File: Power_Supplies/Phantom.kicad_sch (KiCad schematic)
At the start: 24 parts, among them IC9 LT8338, J3 XLR3, SW1 SW_Push

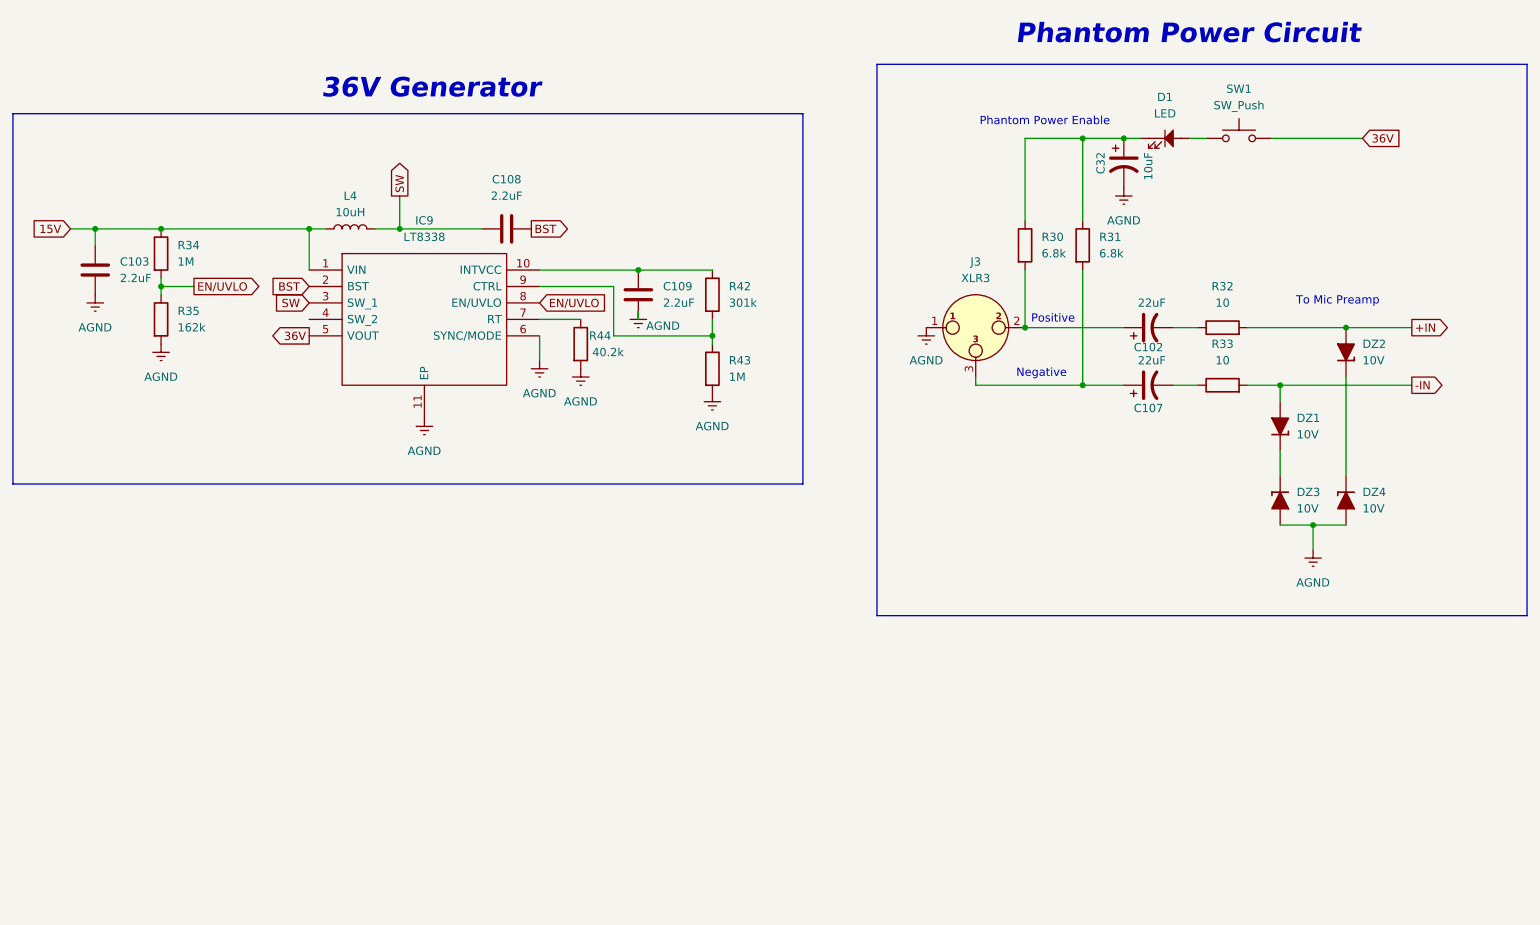
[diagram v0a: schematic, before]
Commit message: Started preamp design (finished stage 1)
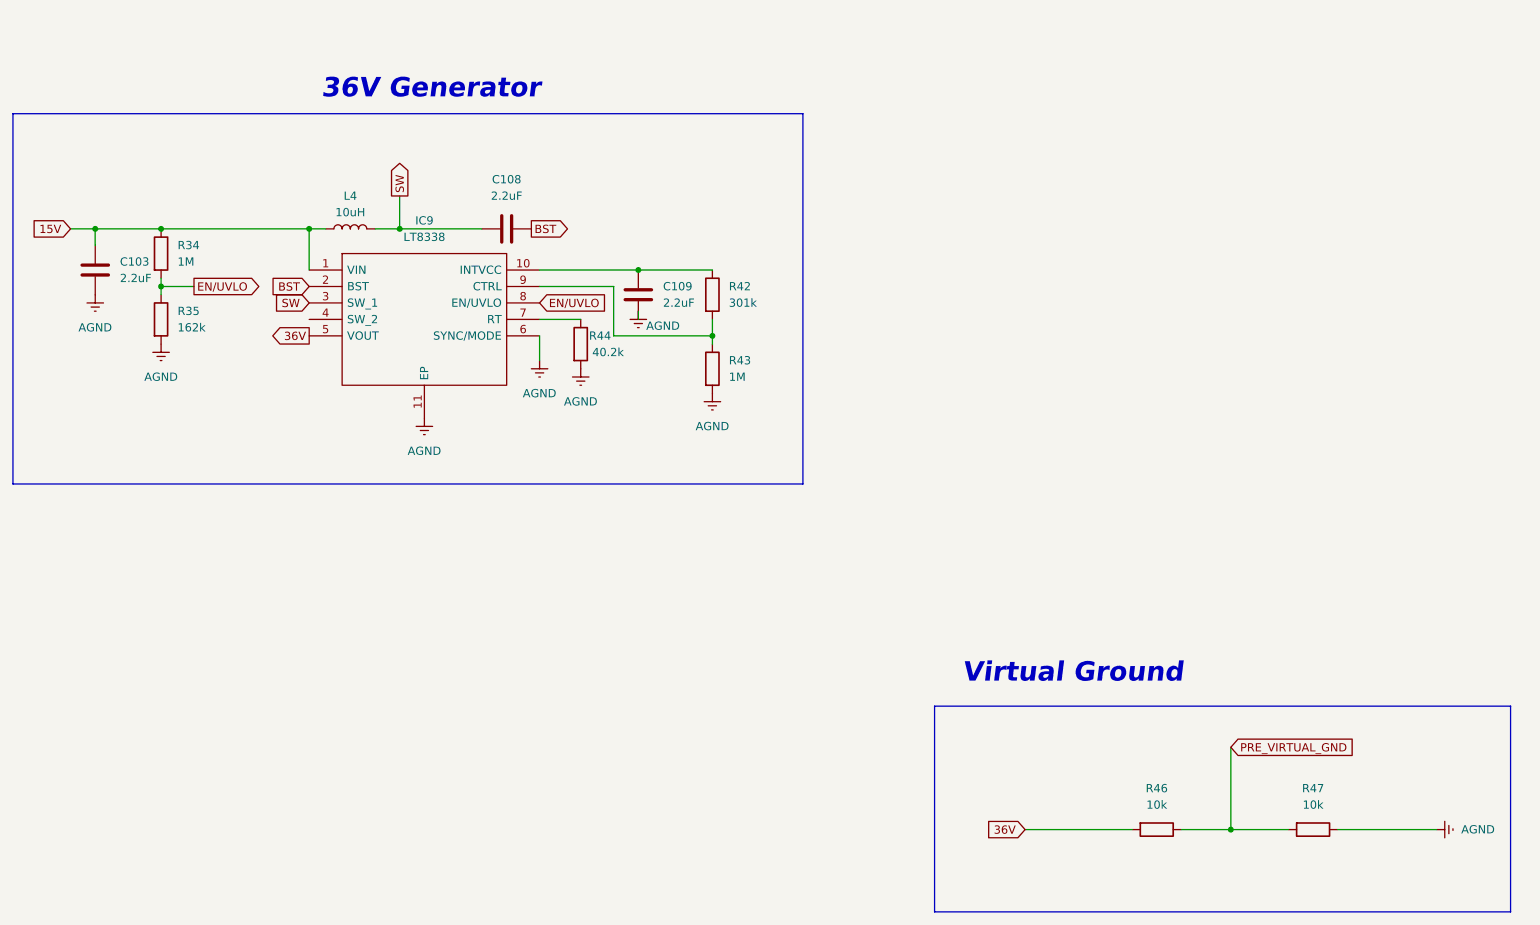
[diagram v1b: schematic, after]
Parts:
- removed C102, C107: 22uF, Capacitor_SMD:CP_Elec_4x5.8, symbol Device:C_Polarized_US
- removed C32: 10uF, Capacitor_SMD:CP_Elec_4x5.8, symbol Device:C_Polarized_US
- removed D1: LED, LED_THT:LED_D5.0mm, symbol PCM_SL_Devices:LED
- removed DZ1, DZ2, DZ3, DZ4: 10V, Diode_SMD:D_SMB, symbol PCM_Diode_Zener_AKL:D_Zener_Generic
- removed J3: XLR3, symbol Connector_Audio:XLR3
- removed R30, R31: 6.8k, Resistor_SMD:R_0805_2012Metric, symbol Device:R
- removed R32, R33: 10, Resistor_SMD:R_0805_2012Metric, symbol Device:R
- removed SW1: SW_Push, Button_Switch_THT:SW_PUSH_1P1T_6x3.5mm_H5.0_APEM_MJTP1250, symbol Switch:SW_Push
- added R46, R47: 10k, Resistor_SMD:R_0805_2012Metric, symbol Device:R
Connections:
- net 36V: now also R46.2
- net AGND: now also R47.1
- new net PRE_VIRTUAL_GND: R46.1, R47.2
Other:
- note added: "Virtual Ground"
- note removed: "Negative"
- note removed: "Phantom Power Circuit"
- note removed: "Phantom Power Enable"
- note removed: "Positive"
- note removed: "To Mic Preamp"
